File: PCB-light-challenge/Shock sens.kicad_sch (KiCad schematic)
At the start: 1 part

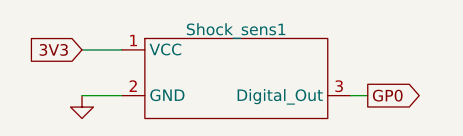
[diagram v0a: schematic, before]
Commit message: TP footprint verandert,  apparte grond (P-) gemaakt.  AC  clearance verandert.  connector voor PIR verandert
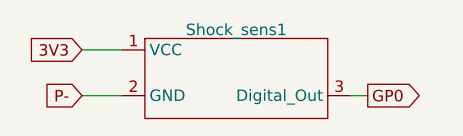
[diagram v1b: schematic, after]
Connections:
- net GND renamed P-
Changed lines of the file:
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@@
     )
   )
-  (symbol (lib_id "power:GND") (at 80.645 71.12 0) (unit 1)
-    (in_bom yes) (on_board yes) (dnp no) (fields_autoplaced)
-    (property "Reference" "#PWR04" (at 80.645 77.47 0)
-      (effects (font (size 1.27 1.27)) hide)
-    )
-    (property "Value" "GND" (at 80.645 75.2555 0)
-      (effects (font (size 1.27 1.27)) hide)
-    )
-    (property "Footprint" "" (at 80.645 71.12 0)
-      (effects (font (size 1.27 1.27)) hide)
-    )
-    (property "Datasheet" "" (at 80.645 71.12 0)
-      (effects (font (size 1.27 1.27)) hide)
-    )
-    (pin "1")
-    (instances
-      (project "PCB-light-challenge"
-        (path "/35573e8f-7834-430c-81d2-239f316c7834/60e08cef-d6ff-4122-9aae-654ea68342de"
-          (reference "#PWR04") (unit 1)
-        )
-      )
+  (global_label "P-" (shape input) (at 80.645 71.12 180) (fields_autoplaced)
+    (effects (font (size 1.27 1.27)) (justify right))
+    (property "Intersheetrefs" "${INTERSHEET_REFS}" (at 74.8968 71.12 0)
+      (effects (font (size 1.27 1.27)) (justify right) hide)
     )
   )

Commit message: Vias  kleiner gemaakt en grond GND genoemd op silkscreen
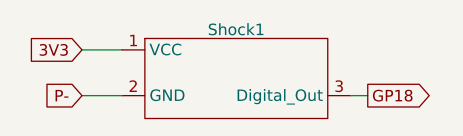
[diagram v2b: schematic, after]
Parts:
- renumbered Shock_sens1 to Shock1
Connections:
- net GP0 renamed GP18
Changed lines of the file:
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@@
     (stroke (width 0) (type default))
   )
-  (global_label "GP0" (shape output) (at 112.395 71.12 0) (fields_autoplaced)
+  (global_label "GP18" (shape output) (at 112.395 71.12 0) (fields_autoplaced)
     (effects (font (size 1.27 1.27)) (justify left))
-    (property "Intersheetrefs" "${INTERSHEET_REFS}" (at 119.0503 71.12 0)
+    (property "Intersheetrefs" "${INTERSHEET_REFS}" (at 120.2598 71.12 0)
       (effects (font (size 1.27 1.27)) (justify left) hide)
     )
@@
   (symbol (lib_id "shock:shock_sens") (at 97.79 63.5 0) (unit 1)
     (in_bom yes) (on_board yes) (dnp no) (fields_autoplaced)
-    (property "Reference" "Shock_sens1" (at 97.79 63.8081 0)
+    (property "Reference" "Shock1" (at 97.79 63.8081 0)
       (effects (font (size 1.27 1.27)))
     )
@@
       (project "PCB-light-challenge"
         (path "/35573e8f-7834-430c-81d2-239f316c7834/60e08cef-d6ff-4122-9aae-654ea68342de"
-          (reference "Shock_sens1") (unit 1)
+          (reference "Shock1") (unit 1)
         )
       )

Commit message: 3V3 OUT voor RGB toegevoegd en footprint van connectoren verandert naar JST
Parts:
- Shock1: footprint Connector_PinHeader_2.54mm:PinHeader_1x03_P2.54mm_Vertical -> Connector_JST:JST_EH_B3B-EH-A_1x03_P2.50mm_Vertical
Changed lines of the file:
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@@
       (effects (font (size 1.27 1.27)))
     )
-    (property "Footprint" "Connector_PinHeader_2.54mm:PinHeader_1x03_P2.54mm_Vertical" (at 97.79 63.5 0)
+    (property "Footprint" "Connector_JST:JST_EH_B3B-EH-A_1x03_P2.50mm_Vertical" (at 97.79 63.5 0)
       (effects (font (size 1.27 1.27)) hide)
     )
